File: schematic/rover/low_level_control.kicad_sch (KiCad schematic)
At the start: 0 parts

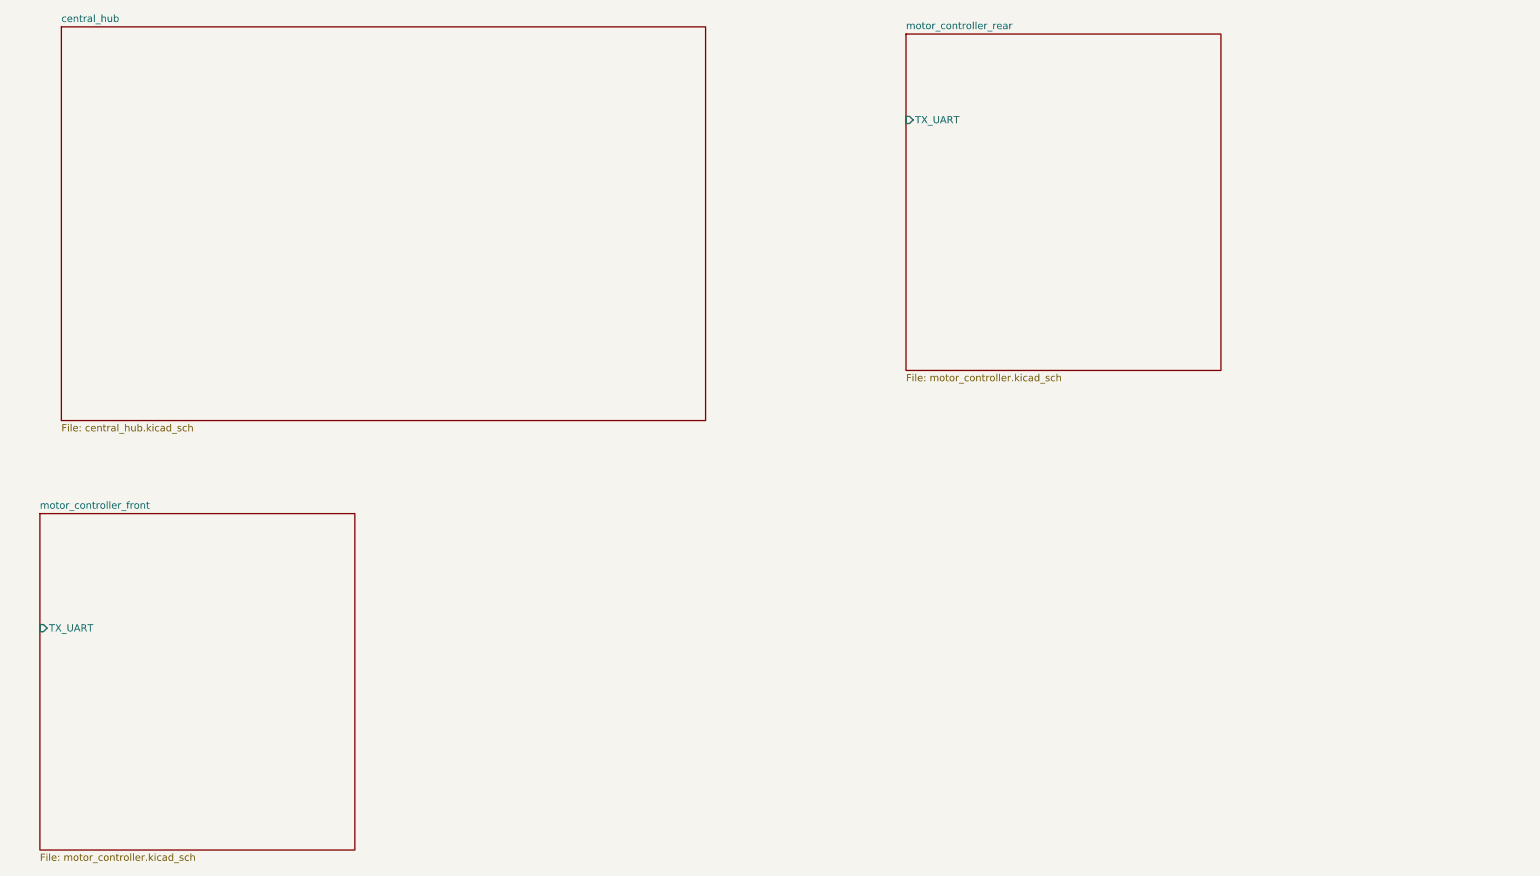
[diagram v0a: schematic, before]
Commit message: Complete motor controller schematic
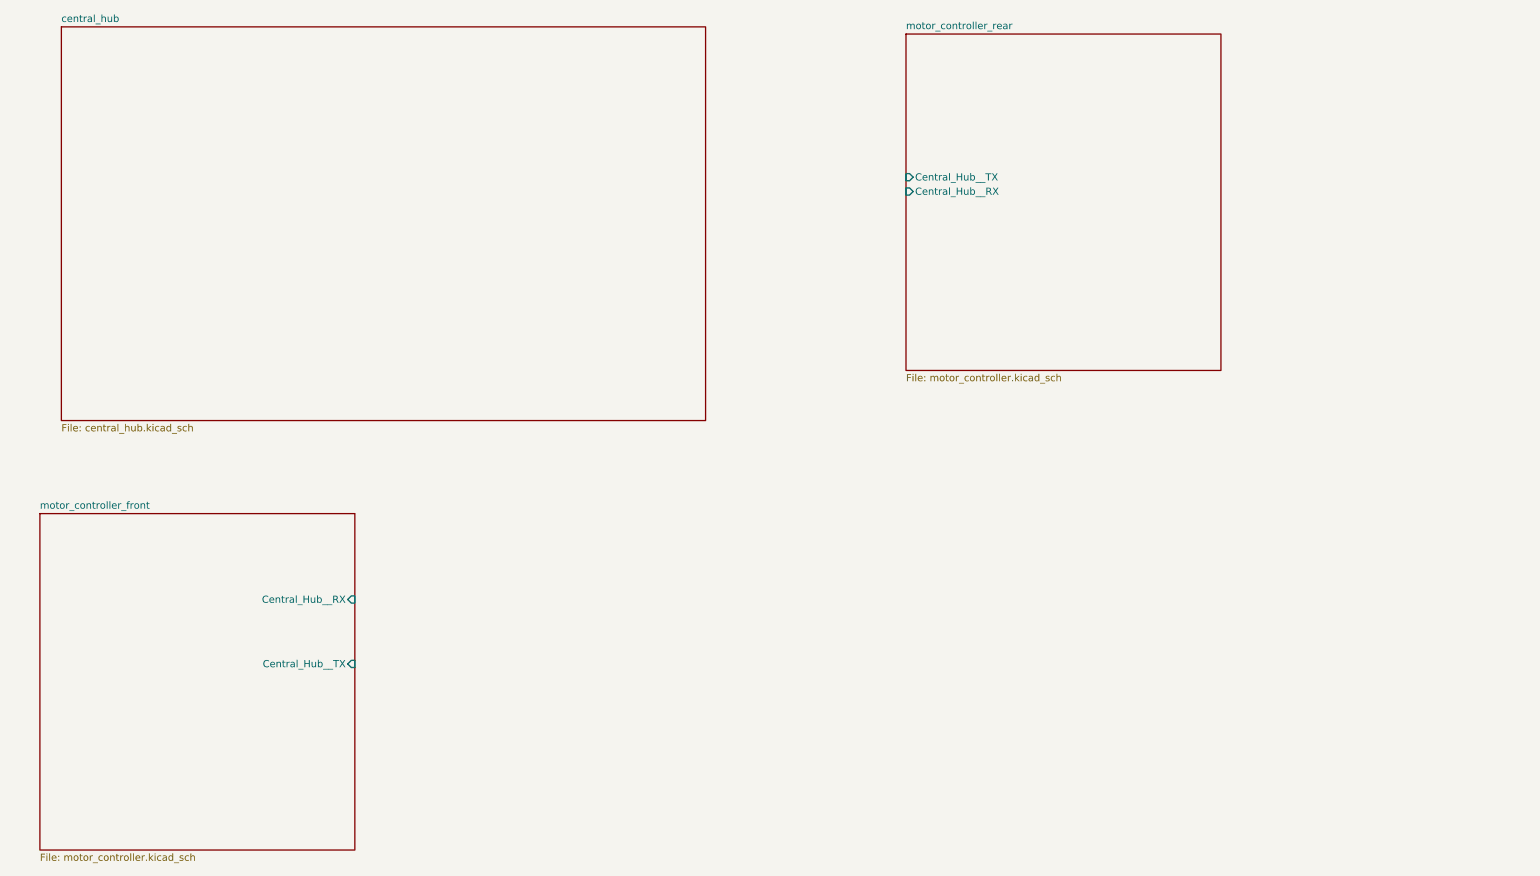
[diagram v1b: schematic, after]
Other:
- sheet motor_controller_front ports: added Central_Hub__RX, Central_Hub__TX; removed TX_UART
- sheet motor_controller_rear ports: added Central_Hub__RX, Central_Hub__TX; removed TX_UART
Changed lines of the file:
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@@
       (effects (font (size 1.27 1.27)) (justify left top))
     )
-    (pin "TX_UART" input (at 19.05 132.08 180)
-      (effects (font (size 1.27 1.27)) (justify left))
+    (pin "Central_Hub__RX" input (at 74.93 127 0)
+      (effects (font (size 1.27 1.27)) (justify right))
+    )
+    (pin "Central_Hub__TX" input (at 74.93 138.43 0)
+      (effects (font (size 1.27 1.27)) (justify right))
     )
     (instances
@@
       (effects (font (size 1.27 1.27)) (justify left top))
     )
-    (pin "TX_UART" input (at 172.72 41.91 180)
+    (pin "Central_Hub__RX" input (at 172.72 54.61 180)
       (effects (font (size 1.27 1.27)) (justify left))
     )
+    (pin "Central_Hub__TX" input (at 172.72 52.07 180)
+      (effects (font (size 1.27 1.27)) (justify left))
+    )

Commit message: Complete Central Hub schematic
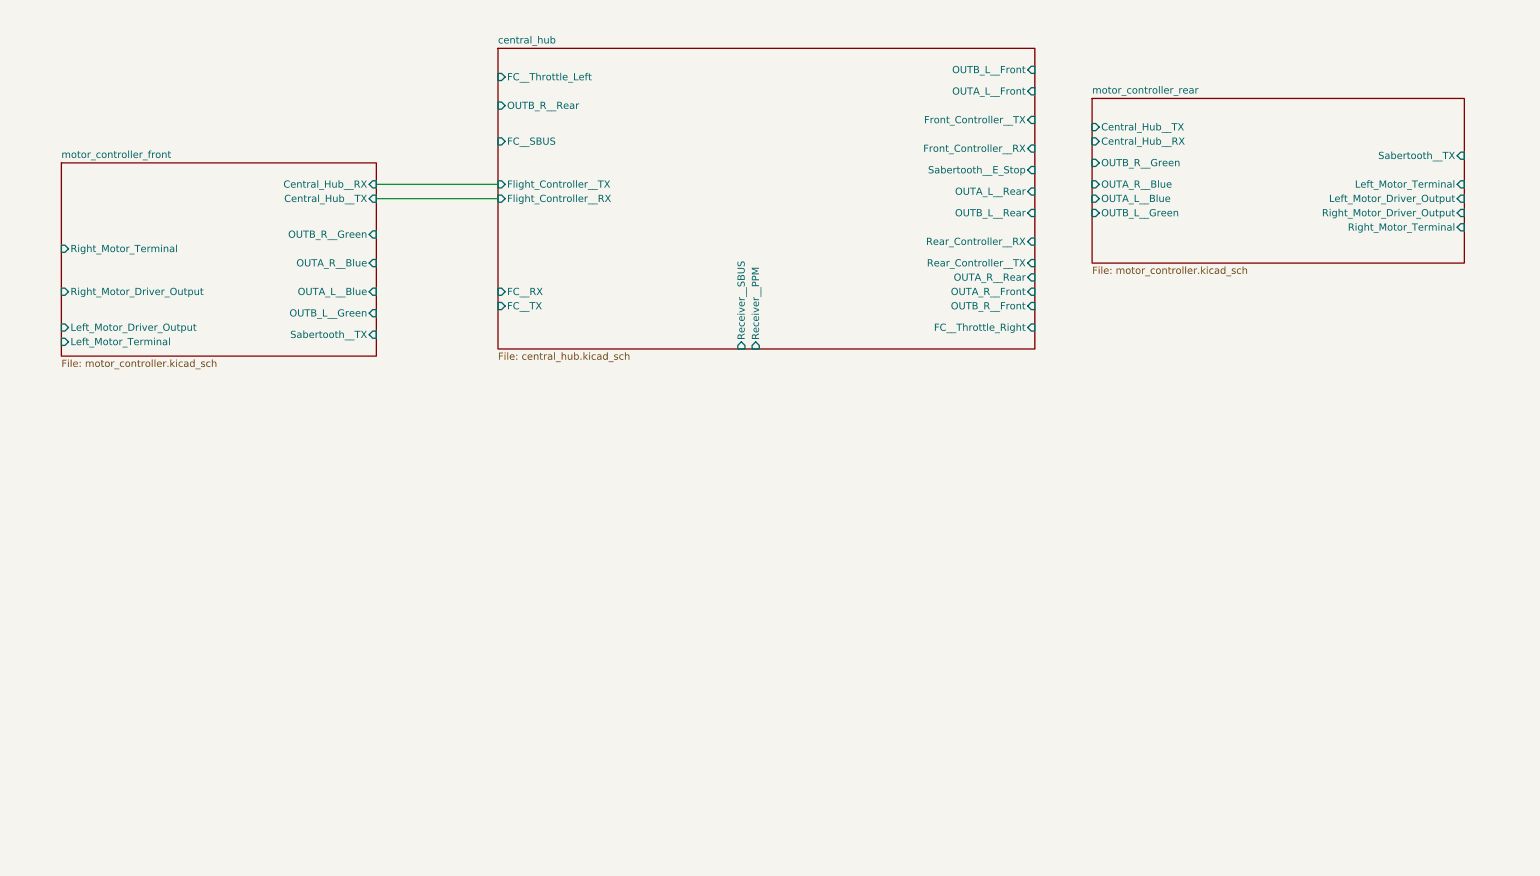
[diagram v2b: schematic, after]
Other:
- sheet central_hub ports: added FC__RX, FC__SBUS, FC__TX, FC__Throttle_Left, FC__Throttle_Right, Flight_Controller__RX, Flight_Controller__TX, Front_Controller__RX, Front_Controller__TX, OUTA_L__Front, OUTA_L__Rear, OUTA_R__Front, OUTA_R__Rear, OUTB_L__Front, OUTB_L__Rear, OUTB_R__Front, OUTB_R__Rear, Rear_Controller__RX, Rear_Controller__TX, Receiver__PPM, Receiver__SBUS, Sabertooth__E_Stop; removed none
- sheet motor_controller_front ports: added Left_Motor_Driver_Output, Left_Motor_Terminal, OUTA_L__Blue, OUTA_R__Blue, OUTB_L__Green, OUTB_R__Green, Right_Motor_Driver_Output, Right_Motor_Terminal, Sabertooth__TX; removed none
- sheet motor_controller_rear ports: added Left_Motor_Driver_Output, Left_Motor_Terminal, OUTA_L__Blue, OUTA_R__Blue, OUTB_L__Green, OUTB_R__Green, Right_Motor_Driver_Output, Right_Motor_Terminal, Sabertooth__TX; removed none
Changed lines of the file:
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@@
 (kicad_sch (version 20230121) (generator eeschema)
   (paper "A4")
-  (sheet (at 19.05 111.76) (size 55.88 59.69) (fields_autoplaced)
+  (wire (pts (xy 78.74 55.88) (xy 100.33 55.88))
+    (stroke (width 0) (type default))
+  )
+  (wire (pts (xy 78.74 53.34) (xy 100.33 53.34))
+    (stroke (width 0) (type default))
+  )
+  (sheet (at 22.86 49.53) (size 55.88 34.29) (fields_autoplaced)
     (stroke (width 0.1524) (type solid))
     (fill (color 0 0 0 0.0000))
-    (property "Sheetname" "motor_controller_front" (at 19.05 111.0484 0)
+    (property "Sheetname" "motor_controller_front" (at 22.86 48.8184 0)
       (effects (font (size 1.27 1.27)) (justify left bottom))
     )
-    (property "Sheetfile" "motor_controller.kicad_sch" (at 19.05 172.0346 0)
+    (property "Sheetfile" "motor_controller.kicad_sch" (at 22.86 84.4046 0)
       (effects (font (size 1.27 1.27)) (justify left top))
     )
-    (pin "Central_Hub__RX" input (at 74.93 127 0)
+    (pin "Central_Hub__RX" input (at 78.74 53.34 0)
       (effects (font (size 1.27 1.27)) (justify right))
     )
-    (pin "Central_Hub__TX" input (at 74.93 138.43 0)
+    (pin "Central_Hub__TX" input (at 78.74 55.88 0)
       (effects (font (size 1.27 1.27)) (justify right))
+    )
+    (pin "OUTB_R__Green" input (at 78.74 62.23 0)
+      (effects (font (size 1.27 1.27)) (justify right))
+    )
+    (pin "OUTA_R__Blue" input (at 78.74 67.31 0)
+      (effects (font (size 1.27 1.27)) (justify right))
+    )
+    (pin "OUTA_L__Blue" input (at 78.74 72.39 0)
+      (effects (font (size 1.27 1.27)) (justify right))
+    )
+    (pin "OUTB_L__Green" input (at 78.74 76.2 0)
+      (effects (font (size 1.27 1.27)) (justify right))
+    )
+    (pin "Sabertooth__TX" input (at 78.74 80.01 0)
+      (effects (font (size 1.27 1.27)) (justify right))
+    )
+    (pin "Left_Motor_Terminal" input (at 22.86 81.28 180)
+      (effects (font (size 1.27 1.27)) (justify left))
+    )
+    (pin "Left_Motor_Driver_Output" input (at 22.86 78.74 180)
+      (effects (font (size 1.27 1.27)) (justify left))
+    )
+    (pin "Right_Motor_Driver_Output" input (at 22.86 72.39 180)
+      (effects (font (size 1.27 1.27)) (justify left))
+    )
+    (pin "Right_Motor_Terminal" input (at 22.86 64.77 180)
+      (effects (font (size 1.27 1.27)) (justify left))
     )
     (instances
@@
     )
   )
-  (sheet (at 172.72 26.67) (size 55.88 59.69) (fields_autoplaced)
+  (sheet (at 205.74 38.1) (size 66.04 29.21) (fields_autoplaced)
     (stroke (width 0.1524) (type solid))
     (fill (color 0 0 0 0.0000))
-    (property "Sheetname" "motor_controller_rear" (at 172.72 25.9584 0)
+    (property "Sheetname" "motor_controller_rear" (at 205.74 37.3884 0)
       (effects (font (size 1.27 1.27)) (justify left bottom))
     )
-    (property "Sheetfile" "motor_controller.kicad_sch" (at 172.72 86.9446 0)
+    (property "Sheetfile" "motor_controller.kicad_sch" (at 205.74 67.8946 0)
       (effects (font (size 1.27 1.27)) (justify left top))
     )
-    (pin "Central_Hub__RX" input (at 172.72 54.61 180)
+    (pin "Central_Hub__RX" input (at 205.74 45.72 180)
       (effects (font (size 1.27 1.27)) (justify left))
     )
-    (pin "Central_Hub__TX" input (at 172.72 52.07 180)
+    (pin "Central_Hub__TX" input (at 205.74 43.18 180)
       (effects (font (size 1.27 1.27)) (justify left))
+    )
+    (pin "OUTB_R__Green" input (at 205.74 49.53 180)
+      (effects (font (size 1.27 1.27)) (justify left))
+    )
+    (pin "OUTA_R__Blue" input (at 205.74 53.34 180)
+      (effects (font (size 1.27 1.27)) (justify left))
+    )
+    (pin "OUTA_L__Blue" input (at 205.74 55.88 180)
+      (effects (font (size 1.27 1.27)) (justify left))
+    )
+    (pin "OUTB_L__Green" input (at 205.74 58.42 180)
+      (effects (font (size 1.27 1.27)) (justify left))
+    )
+    (pin "Sabertooth__TX" input (at 271.78 48.26 0)
+      (effects (font (size 1.27 1.27)) (justify right))
+    )
+    (pin "Left_Motor_Terminal" input (at 271.78 53.34 0)
+      (effects (font (size 1.27 1.27)) (justify right))
+    )
+    (pin "Left_Motor_Driver_Output" input (at 271.78 55.88 0)
+      (effects (font (size 1.27 1.27)) (justify right))
+    )
+    (pin "Right_Motor_Driver_Output" input (at 271.78 58.42 0)
+      (effects (font (size 1.27 1.27)) (justify right))
+    )
+    (pin "Right_Motor_Terminal" input (at 271.78 60.96 0)
+      (effects (font (size 1.27 1.27)) (justify right))
     )
     (instances
@@
     )
   )
-  (sheet (at 22.86 25.4) (size 114.3 69.85) (fields_autoplaced)
+  (sheet (at 100.33 29.21) (size 95.25 53.34) (fields_autoplaced)
     (stroke (width 0.1524) (type solid))
     (fill (color 0 0 0 0.0000))
-    (property "Sheetname" "central_hub" (at 22.86 24.6884 0)
+    (property "Sheetname" "central_hub" (at 100.33 28.4984 0)
       (effects (font (size 1.27 1.27)) (justify left bottom))
     )
-    (property "Sheetfile" "central_hub.kicad_sch" (at 22.86 95.8346 0)
+    (property "Sheetfile" "central_hub.kicad_sch" (at 100.33 83.1346 0)
       (effects (font (size 1.27 1.27)) (justify left top))
     )
+    (pin "OUTB_L__Front" input (at 195.58 33.02 0)
+      (effects (font (size 1.27 1.27)) (justify right))
+    )
+    (pin "OUTA_L__Front" input (at 195.58 36.83 0)
+      (effects (font (size 1.27 1.27)) (justify right))
+    )
+    (pin "Front_Controller__TX" input (at 195.58 41.91 0)
+      (effects (font (size 1.27 1.27)) (justify right))
+    )
+    (pin "Front_Controller__RX" input (at 195.58 46.99 0)
+      (effects (font (size 1.27 1.27)) (justify right))
+    )
+    (pin "Sabertooth__E_Stop" input (at 195.58 50.8 0)
+      (effects (font (size 1.27 1.27)) (justify right))
+    )
+    (pin "OUTA_L__Rear" input (at 195.58 54.61 0)
+      (effects (font (size 1.27 1.27)) (justify right))
+    )
+    (pin "OUTB_L__Rear" input (at 195.58 58.42 0)
+      (effects (font (size 1.27 1.27)) (justify right))
+    )
+    (pin "Rear_Controller__RX" input (at 195.58 63.5 0)
+      (effects (font (size 1.27 1.27)) (justify right))
+    )
+    (pin "Rear_Controller__TX" input (at 195.58 67.31 0)
+      (effects (font (size 1.27 1.27)) (justify right))
+    )
+    (pin "OUTA_R__Rear" input (at 195.58 69.85 0)
+      (effects (font (size 1.27 1.27)) (justify right))
+    )
+    (pin "OUTA_R__Front" input (at 195.58 72.39 0)
+      (effects (font (size 1.27 1.27)) (justify right))
+    )
+    (pin "OUTB_R__Front" input (at 195.58 74.93 0)
+      (effects (font (size 1.27 1.27)) (justify right))
+    )
+    (pin "FC__Throttle_Right" input (at 195.58 78.74 0)
+      (effects (font (size 1.27 1.27)) (justify right))
+    )
+    (pin "FC__Throttle_Left" input (at 100.33 34.29 180)
+      (effects (font (size 1.27 1.27)) (justify left))
+    )
+    (pin "OUTB_R__Rear" input (at 100.33 39.37 180)
+      (effects (font (size 1.27 1.27)) (justify left))
+    )
+    (pin "FC__SBUS" input (at 100.33 45.72 180)
+      (effects (font (size 1.27 1.27)) (justify left))
+    )
+    (pin "Flight_Controller__TX" input (at 100.33 53.34 180)
+      (effects (font (size 1.27 1.27)) (justify left))
+    )
+    (pin "Flight_Controller__RX" input (at 100.33 55.88 180)
+      (effects (font (size 1.27 1.27)) (justify left))
+    )
+    (pin "Receiver__PPM" input (at 146.05 82.55 270)
+      (effects (font (size 1.27 1.27)) (justify left))
+    )
+    (pin "Receiver__SBUS" input (at 143.51 82.55 270)
+      (effects (font (size 1.27 1.27)) (justify left))
+    )
+    (pin "FC__RX" input (at 100.33 72.39 180)
+      (effects (font (size 1.27 1.27)) (justify left))
+    )
+    (pin "FC__TX" input (at 100.33 74.93 180)
+      (effects (font (size 1.27 1.27)) (justify left))
+    )
     (instances

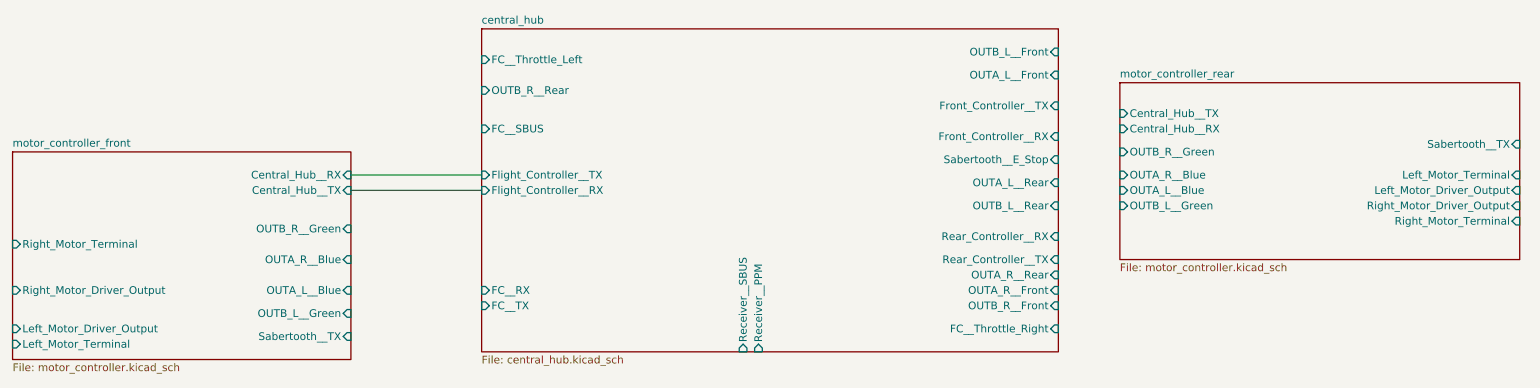
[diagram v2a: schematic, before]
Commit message: Update connection between picos
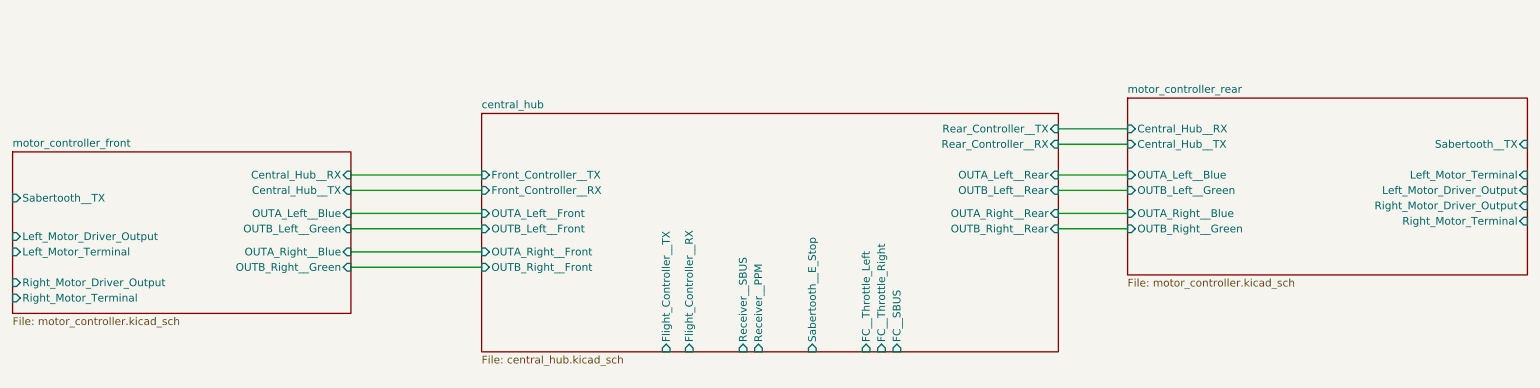
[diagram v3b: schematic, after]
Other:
- sheet central_hub ports: added OUTA_Left__Front, OUTA_Left__Rear, OUTA_Right__Front, OUTA_Right__Rear, OUTB_Left__Front, OUTB_Left__Rear, OUTB_Right__Front, OUTB_Right__Rear; removed FC__RX, FC__TX, OUTA_L__Front, OUTA_L__Rear, OUTA_R__Front, OUTA_R__Rear, OUTB_L__Front, OUTB_L__Rear, OUTB_R__Front, OUTB_R__Rear
- sheet motor_controller_front ports: added OUTA_Left__Blue, OUTA_Right__Blue, OUTB_Left__Green, OUTB_Right__Green; removed OUTA_L__Blue, OUTA_R__Blue, OUTB_L__Green, OUTB_R__Green
- sheet motor_controller_rear ports: added OUTA_Left__Blue, OUTA_Right__Blue, OUTB_Left__Green, OUTB_Right__Green; removed OUTA_L__Blue, OUTA_R__Blue, OUTB_L__Green, OUTB_R__Green
